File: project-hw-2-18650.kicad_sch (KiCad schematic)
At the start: 2 parts, among them J2 2060-452_998-404

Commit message: pcb: first draft
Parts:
- renumbered J2 to J1
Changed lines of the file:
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@@
 		(dnp no)
 		(fields_autoplaced yes)
-		(property "Reference" "#PWR04"
+		(property "Reference" "#PWR03"
 			(at 60.96 29.21 0)
 			(effects
@@
 			(project "project-hw-2-18650"
 				(path "/95204d1f-789d-4da7-bef1-75eceb67dba1"
-					(reference "#PWR04")
+					(reference "#PWR03")
 					(unit 1)
 				)
@@
 		(dnp no)
 		(fields_autoplaced yes)
-		(property "Reference" "#PWR05"
+		(property "Reference" "#PWR04"
 			(at 60.96 48.26 0)
 			(effects
@@
 			(project "project-hw-2-18650"
 				(path "/95204d1f-789d-4da7-bef1-75eceb67dba1"
-					(reference "#PWR05")
+					(reference "#PWR04")
 					(unit 1)
 				)
@@
 		(dnp no)
 		(fields_autoplaced yes)
-		(property "Reference" "#PWR02"
+		(property "Reference" "#PWR01"
 			(at 22.86 29.21 0)
 			(effects
@@
 			(project ""
 				(path "/95204d1f-789d-4da7-bef1-75eceb67dba1"
-					(reference "#PWR02")
+					(reference "#PWR01")
 					(unit 1)
 				)
@@
 		(dnp no)
 		(fields_autoplaced yes)
-		(property "Reference" "J2"
+		(property "Reference" "J1"
 			(at 124.46 27.9399 0)
 			(effects
@@
 			(project ""
 				(path "/95204d1f-789d-4da7-bef1-75eceb67dba1"
-					(reference "J2")
+					(reference "J1")
 					(unit 1)
 				)
@@
 		(dnp no)
 		(fields_autoplaced yes)
-		(property "Reference" "#PWR01"
+		(property "Reference" "#PWR02"
 			(at 22.86 48.26 0)
 			(effects
@@
 			(project ""
 				(path "/95204d1f-789d-4da7-bef1-75eceb67dba1"
-					(reference "#PWR01")
+					(reference "#PWR02")
 					(unit 1)
 				)
@@
 		(dnp no)
 		(fields_autoplaced yes)
-		(property "Reference" "#PWR03"
+		(property "Reference" "#PWR05"
 			(at 106.68 48.26 0)
 			(effects
@@
 			(project "project-hw-2-18650"
 				(path "/95204d1f-789d-4da7-bef1-75eceb67dba1"
-					(reference "#PWR03")
+					(reference "#PWR05")
 					(unit 1)
 				)

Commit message: pcb: add ground backplane
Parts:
- added H1, H2: MountingHole_Pad, MountingHole:MountingHole_3.2mm_M3_ISO14580_Pad, symbol Mechanical:MountingHole_Pad
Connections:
- net GND: now also H1.1, H2.1
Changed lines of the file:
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@@
 	(generator_version "8.0")
 	(paper "A4")
+	(junction
+		(at 236.22 29.21)
+		(diameter 0)
+		(color 0 0 0 0)
+	)
 	(wire
 		(pts
@@
 	(wire
 		(pts
+			(xy 243.84 29.21) (xy 236.22 29.21)
+		)
+		(stroke
+			(width 0)
+			(type default)
+		)
+	)
+	(wire
+		(pts
 			(xy 60.96 27.94) (xy 67.31 27.94)
 		)
@@
 	(wire
 		(pts
+			(xy 236.22 22.86) (xy 236.22 29.21)
+		)
+		(stroke
+			(width 0)
+			(type default)
+		)
+	)
+	(wire
+		(pts
 			(xy 22.86 31.75) (xy 30.48 31.75)
 		)
@@
 	(wire
 		(pts
+			(xy 243.84 22.86) (xy 236.22 22.86)
+		)
+		(stroke
+			(width 0)
+			(type default)
+		)
+	)
+	(wire
+		(pts
 			(xy 106.68 41.91) (xy 106.68 30.48)
+		)
+		(stroke
+			(width 0)
+			(type default)
+		)
+	)
+	(wire
+		(pts
+			(xy 236.22 29.21) (xy 236.22 34.29)
 		)
 		(stroke
@@
 	)
 	(symbol
+		(lib_id "Mechanical:MountingHole_Pad")
+		(at 246.38 29.21 270)
+		(unit 1)
+		(exclude_from_sim yes)
+		(in_bom no)
+		(on_board yes)
+		(dnp no)
+		(fields_autoplaced yes)
+		(property "Reference" "H2"
+			(at 250.19 27.9399 90)
+			(effects
+				(font
+					(size 1.27 1.27)
+				)
+				(justify left)
+			)
+		)
+		(property "Value" "MountingHole_Pad"
+			(at 250.19 30.4799 90)
+			(effects
+				(font
+					(size 1.27 1.27)
+				)
+				(justify left)
+			)
+		)
+		(property "Footprint" "MountingHole:MountingHole_3.2mm_M3_ISO14580_Pad"
+			(at 246.38 29.21 0)
+			(effects
+				(font
+					(size 1.27 1.27)
+				)
+				(hide yes)
+			)
+		)
+		(property "Datasheet" "~"
+			(at 246.38 29.21 0)
+			(effects
+				(font
+					(size 1.27 1.27)
+				)
+				(hide yes)
+			)
+		)
+		(property "Description" "Mounting Hole with connection"
+			(at 246.38 29.21 0)
+			(effects
+				(font
+					(size 1.27 1.27)
+				)
+				(hide yes)
+			)
+		)
+		(pin "1"
+		)
+		(instances
+			(project "project-hw-2-18650"
+				(path "/95204d1f-789d-4da7-bef1-75eceb67dba1"
+					(reference "H2")
+					(unit 1)
+				)
+			)
+		)
+	)
+	(symbol
+		(lib_id "Mechanical:MountingHole_Pad")
+		(at 246.38 22.86 270)
+		(unit 1)
+		(exclude_from_sim yes)
+		(in_bom no)
+		(on_board yes)
+		(dnp no)
+		(fields_autoplaced yes)
+		(property "Reference" "H1"
+			(at 250.19 21.5899 90)
+			(effects
+				(font
+					(size 1.27 1.27)
+				)
+				(justify left)
+			)
+		)
+		(property "Value" "MountingHole_Pad"
+			(at 250.19 24.1299 90)
+			(effects
+				(font
+					(size 1.27 1.27)
+				)
+				(justify left)
+			)
+		)
+		(property "Footprint" "MountingHole:MountingHole_3.2mm_M3_ISO14580_Pad"
+			(at 246.38 22.86 0)
+			(effects
+				(font
+					(size 1.27 1.27)
+				)
+				(hide yes)
+			)
+		)
+		(property "Datasheet" "~"
+			(at 246.38 22.86 0)
+			(effects
+				(font
+					(size 1.27 1.27)
+				)
+				(hide yes)
+			)
+		)
+		(property "Description" "Mounting Hole with connection"
+			(at 246.38 22.86 0)
+			(effects
+				(font
+					(size 1.27 1.27)
+				)
+				(hide yes)
+			)
+		)
+		(pin "1"
+		)
+		(instances
+			(project "project-hw-2-18650"
+				(path "/95204d1f-789d-4da7-bef1-75eceb67dba1"
+					(reference "H1")
+					(unit 1)
+				)
+			)
+		)
+	)
+	(symbol
 		(lib_id "2060-452_998-404:2060-452_998-404")
 		(at 118.11 30.48 0)
@@
 					(unit 1)
 				)
+			)
+		)
+	)
+	(symbol
+		(lib_id "power:GND")
+		(at 236.22 34.29 0)
+		(unit 1)
+		(exclude_from_sim no)
+		(in_bom yes)
+		(on_board yes)
+		(dnp no)
+		(fields_autoplaced yes)
+		(property "Reference" "#PWR06"
+			(at 236.22 40.64 0)
+			(effects
+				(font
+					(size 1.27 1.27)
+				)
+				(hide yes)
+			)
+		)
+		(property "Value" "GND"
+			(at 236.22 39.37 0)
+			(effects
+				(font
+					(size 1.27 1.27)
+				)
+			)
+		)
+		(property "Footprint" ""
+			(at 236.22 34.29 0)
+			(effects
+				(font
+					(size 1.27 1.27)
+				)
+				(hide yes)
+			)
+		)
+		(property "Datasheet" ""
+			(at 236.22 34.29 0)
+			(effects
+				(font
+					(size 1.27 1.27)
+				)
+				(hide yes)
+			)
+		)
+		(property "Description" "Power symbol creates a global label with name \"GND\" , ground"
+			(at 236.22 34.29 0)
+			(effects
+				(font
+					(size 1.27 1.27)
+				)
+				(hide yes)
+			)
+		)
+		(pin "1"
+		)
+		(instances
+			(project "project-hw-2-18650"
+				(path "/95204d1f-789d-4da7-bef1-75eceb67dba1"
+					(reference "#PWR06")
+					(unit 1)
+				)

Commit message: pcb: routing v2
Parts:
- removed H1: MountingHole_Pad, MountingHole:MountingHole_3.2mm_M3_ISO14580_Pad, symbol Mechanical:MountingHole_Pad
- added H1: MountingHole, MountingHole:MountingHole_3.2mm_M3_ISO14580, symbol Mechanical:MountingHole
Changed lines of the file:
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@@
 	(generator_version "8.0")
 	(paper "A4")
-	(junction
-		(at 236.22 29.21)
-		(diameter 0)
-		(color 0 0 0 0)
-	)
 	(wire
 		(pts
@@
 	(wire
 		(pts
-			(xy 236.22 22.86) (xy 236.22 29.21)
-		)
-		(stroke
-			(width 0)
-			(type default)
-		)
-	)
-	(wire
-		(pts
 			(xy 22.86 31.75) (xy 30.48 31.75)
-		)
-		(stroke
-			(width 0)
-			(type default)
-		)
-	)
-	(wire
-		(pts
-			(xy 243.84 22.86) (xy 236.22 22.86)
 		)
 		(stroke
@@
 	)
 	(symbol
-		(lib_id "Mechanical:MountingHole_Pad")
-		(at 246.38 22.86 270)
-		(unit 1)
-		(exclude_from_sim yes)
-		(in_bom no)
-		(on_board yes)
-		(dnp no)
-		(fields_autoplaced yes)
-		(property "Reference" "H1"
-			(at 250.19 21.5899 90)
-			(effects
-				(font
-					(size 1.27 1.27)
-				)
-				(justify left)
-			)
-		)
-		(property "Value" "MountingHole_Pad"
-			(at 250.19 24.1299 90)
-			(effects
-				(font
-					(size 1.27 1.27)
-				)
-				(justify left)
-			)
-		)
-		(property "Footprint" "MountingHole:MountingHole_3.2mm_M3_ISO14580_Pad"
-			(at 246.38 22.86 0)
-			(effects
-				(font
-					(size 1.27 1.27)
-				)
-				(hide yes)
-			)
-		)
-		(property "Datasheet" "~"
-			(at 246.38 22.86 0)
-			(effects
-				(font
-					(size 1.27 1.27)
-				)
-				(hide yes)
-			)
-		)
-		(property "Description" "Mounting Hole with connection"
-			(at 246.38 22.86 0)
-			(effects
-				(font
-					(size 1.27 1.27)
-				)
-				(hide yes)
-			)
-		)
-		(pin "1"
-		)
-		(instances
-			(project "project-hw-2-18650"
-				(path "/95204d1f-789d-4da7-bef1-75eceb67dba1"
-					(reference "H1")
-					(unit 1)
-				)
-			)
-		)
-	)
-	(symbol
 		(lib_id "2060-452_998-404:2060-452_998-404")
 		(at 118.11 30.48 0)
@@
 					(unit 1)
 				)
+			)
+		)
+	)
+	(symbol
+		(lib_id "Mechanical:MountingHole")
+		(at 247.65 22.86 0)
+		(unit 1)
+		(exclude_from_sim yes)
+		(in_bom no)
+		(on_board yes)
+		(dnp no)
+		(fields_autoplaced yes)
+		(property "Reference" "H1"
+			(at 250.19 21.5899 0)
+			(effects
+				(font
+					(size 1.27 1.27)
+				)
+				(justify left)
+			)
+		)
+		(property "Value" "MountingHole"
+			(at 250.19 24.1299 0)
+			(effects
+				(font
+					(size 1.27 1.27)
+				)
+				(justify left)
+			)
+		)
+		(property "Footprint" "MountingHole:MountingHole_3.2mm_M3_ISO14580"
+			(at 247.65 22.86 0)
+			(effects
+				(font
+					(size 1.27 1.27)
+				)
+				(hide yes)
+			)
+		)
+		(property "Datasheet" "~"
+			(at 247.65 22.86 0)
+			(effects
+				(font
+					(size 1.27 1.27)
+				)
+				(hide yes)
+			)
+		)
+		(property "Description" "Mounting Hole without connection"
+			(at 247.65 22.86 0)
+			(effects
+				(font
+					(size 1.27 1.27)
+				)
+				(hide yes)
+			)
+		)
+		(instances
+			(project ""
+				(path "/95204d1f-789d-4da7-bef1-75eceb67dba1"
+					(reference "H1")
+					(unit 1)
+				)

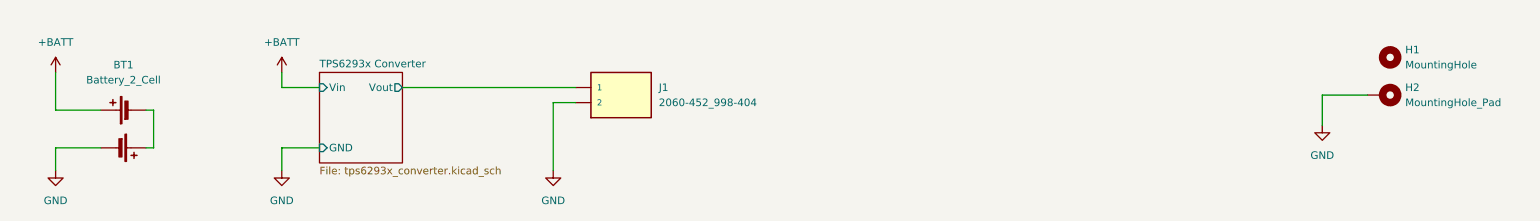
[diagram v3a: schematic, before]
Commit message: sch: add efuse
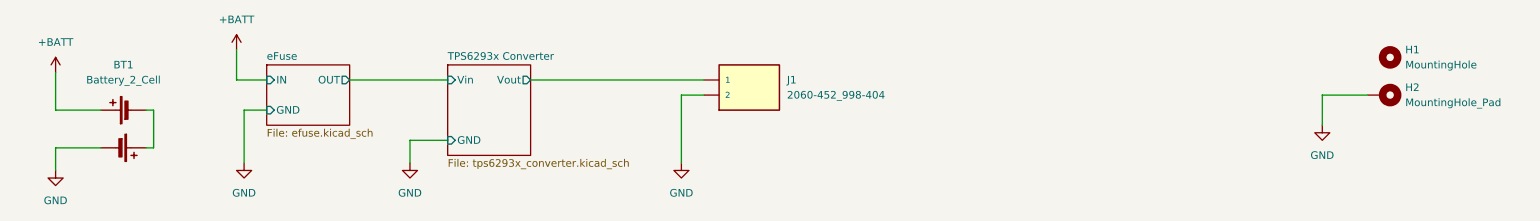
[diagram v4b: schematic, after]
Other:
- added sheet eFuse (efuse.kicad_sch)
- moved on the sheet: J1

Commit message: pcb: first complete routing
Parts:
- removed H1: MountingHole, MountingHole:MountingHole_3.2mm_M3_ISO14580, symbol Mechanical:MountingHole
- removed H2: MountingHole_Pad, MountingHole:MountingHole_3.2mm_M3_ISO14580_Pad, symbol Mechanical:MountingHole_Pad
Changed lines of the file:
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@@
-	(wire
-		(pts
-			(xy 243.84 29.21) (xy 236.22 29.21)
-		)
-		(stroke
-			(width 0)
-			(type default)
-		)
-	)
 	(wire
 		(pts
@@
 		(pts
 			(xy 72.39 26.67) (xy 88.9 26.67)
-		)
-		(stroke
-			(width 0)
-			(type default)
-		)
-	)
-	(wire
-		(pts
-			(xy 236.22 29.21) (xy 236.22 34.29)
 		)
 		(stroke
@@
 	)
 	(symbol
-		(lib_id "Mechanical:MountingHole_Pad")
-		(at 246.38 29.21 270)
-		(unit 1)
-		(exclude_from_sim yes)
-		(in_bom no)
-		(on_board yes)
-		(dnp no)
-		(fields_autoplaced yes)
-		(property "Reference" "H2"
-			(at 250.19 27.9399 90)
-			(effects
-				(font
-					(size 1.27 1.27)
-				)
-				(justify left)
-			)
-		)
-		(property "Value" "MountingHole_Pad"
-			(at 250.19 30.4799 90)
-			(effects
-				(font
-					(size 1.27 1.27)
-				)
-				(justify left)
-			)
-		)
-		(property "Footprint" "MountingHole:MountingHole_3.2mm_M3_ISO14580_Pad"
-			(at 246.38 29.21 0)
-			(effects
-				(font
-					(size 1.27 1.27)
-				)
-				(hide yes)
-			)
-		)
-		(property "Datasheet" "~"
-			(at 246.38 29.21 0)
-			(effects
-				(font
-					(size 1.27 1.27)
-				)
-				(hide yes)
-			)
-		)
-		(property "Description" "Mounting Hole with connection"
-			(at 246.38 29.21 0)
-			(effects
-				(font
-					(size 1.27 1.27)
-				)
-				(hide yes)
-			)
-		)
-		(pin "1"
-		)
-		(instances
-			(project "project-hw-2-18650"
-				(path "/95204d1f-789d-4da7-bef1-75eceb67dba1"
-					(reference "H2")
-					(unit 1)
-				)
-			)
-		)
-	)
-	(symbol
 		(lib_id "2060-452_998-404:2060-452_998-404")
 		(at 139.7 29.21 0)
@@
 	(symbol
 		(lib_id "power:GND")
-		(at 236.22 34.29 0)
-		(unit 1)
-		(exclude_from_sim no)
-		(in_bom yes)
-		(on_board yes)
-		(dnp no)
-		(fields_autoplaced yes)
-		(property "Reference" "#PWR06"
-			(at 236.22 40.64 0)
-			(effects
-				(font
-					(size 1.27 1.27)
-				)
-				(hide yes)
-			)
-		)
-		(property "Value" "GND"
-			(at 236.22 39.37 0)
-			(effects
-				(font
-					(size 1.27 1.27)
-				)
-			)
-		)
-		(property "Footprint" ""
-			(at 236.22 34.29 0)
-			(effects
-				(font
-					(size 1.27 1.27)
-				)
-				(hide yes)
-			)
-		)
-		(property "Datasheet" ""
-			(at 236.22 34.29 0)
-			(effects
-				(font
-					(size 1.27 1.27)
-				)
-				(hide yes)
-			)
-		)
-		(property "Description" "Power symbol creates a global label with name \"GND\" , ground"
-			(at 236.22 34.29 0)
-			(effects
-				(font
-					(size 1.27 1.27)
-				)
-				(hide yes)
-			)
-		)
-		(pin "1"
-		)
-		(instances
-			(project "project-hw-2-18650"
-				(path "/95204d1f-789d-4da7-bef1-75eceb67dba1"
-					(reference "#PWR06")
-					(unit 1)
-				)
-			)
-		)
-	)
-	(symbol
-		(lib_id "power:GND")
 		(at 22.86 41.91 0)
 		(unit 1)
@@
 					(unit 1)
 				)
-			)
-		)
-	)
-	(symbol
-		(lib_id "Mechanical:MountingHole")
-		(at 247.65 22.86 0)
-		(unit 1)
-		(exclude_from_sim yes)
-		(in_bom no)
-		(on_board yes)
-		(dnp no)
-		(fields_autoplaced yes)
-		(property "Reference" "H1"
-			(at 250.19 21.5899 0)
-			(effects
-				(font
-					(size 1.27 1.27)
-				)
-				(justify left)
-			)
-		)
-		(property "Value" "MountingHole"
-			(at 250.19 24.1299 0)
-			(effects
-				(font
-					(size 1.27 1.27)
-				)
-				(justify left)
-			)
-		)
-		(property "Footprint" "MountingHole:MountingHole_3.2mm_M3_ISO14580"
-			(at 247.65 22.86 0)
-			(effects
-				(font
-					(size 1.27 1.27)
-				)
-				(hide yes)
-			)
-		)
-		(property "Datasheet" "~"
-			(at 247.65 22.86 0)
-			(effects
-				(font
-					(size 1.27 1.27)
-				)
-				(hide yes)
-			)
-		)
-		(property "Description" "Mounting Hole without connection"
-			(at 247.65 22.86 0)
-			(effects
-				(font
-					(size 1.27 1.27)
-				)
-				(hide yes)
-			)
-		)
-		(instances
-			(project ""
-				(path "/95204d1f-789d-4da7-bef1-75eceb67dba1"
-					(reference "H1")
-					(unit 1)
-				)

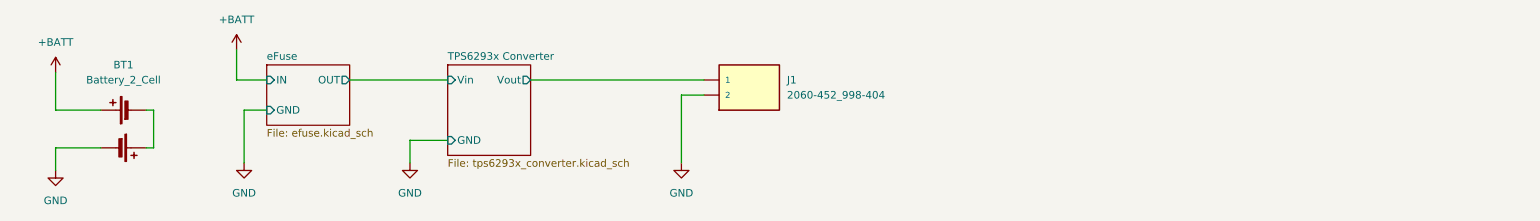
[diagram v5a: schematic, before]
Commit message: sch: add reverse polarity protection
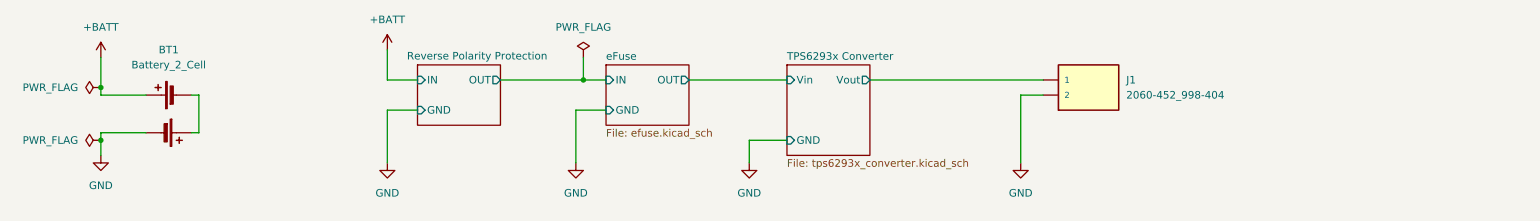
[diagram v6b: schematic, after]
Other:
- added sheet Reverse Polarity Protection (reverse_polarity_protection.kicad_sch)
- moved on the sheet: BT1, J1

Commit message: pcb: route reverse polarity protection
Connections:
- net TPS6293x Converter/Vout renamed buck out
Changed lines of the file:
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@@
+		)
+	)
+	(label "efuse out"
+		(at 130.81 26.67 0)
+		(effects
+			(font
+				(size 1.27 1.27)
+			)
+			(justify left bottom)
+		)
+	)
+	(label "buck out"
+		(at 162.56 26.67 0)
+		(effects
+			(font
+				(size 1.27 1.27)
+			)
+			(justify left bottom)
+		)
+	)
+	(label "pol out"
+		(at 99.06 26.67 0)
+		(effects
+			(font
+				(size 1.27 1.27)
+			)
+			(justify left bottom)
 		)
 	)
